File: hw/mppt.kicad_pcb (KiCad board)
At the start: 4 copper layers, 100.1 x 48.6 mm, 79 parts, among them J201 1935776, J301 1935776, J302 1935776, Q301 SW_L, Q302 SW_H, SW201 SW_Push, U201 MCU_Nucleo_L432KC, U401 INA210, U402 INA210, U403 OPA990, U404 OPA990, U501 LMG1210RVRT

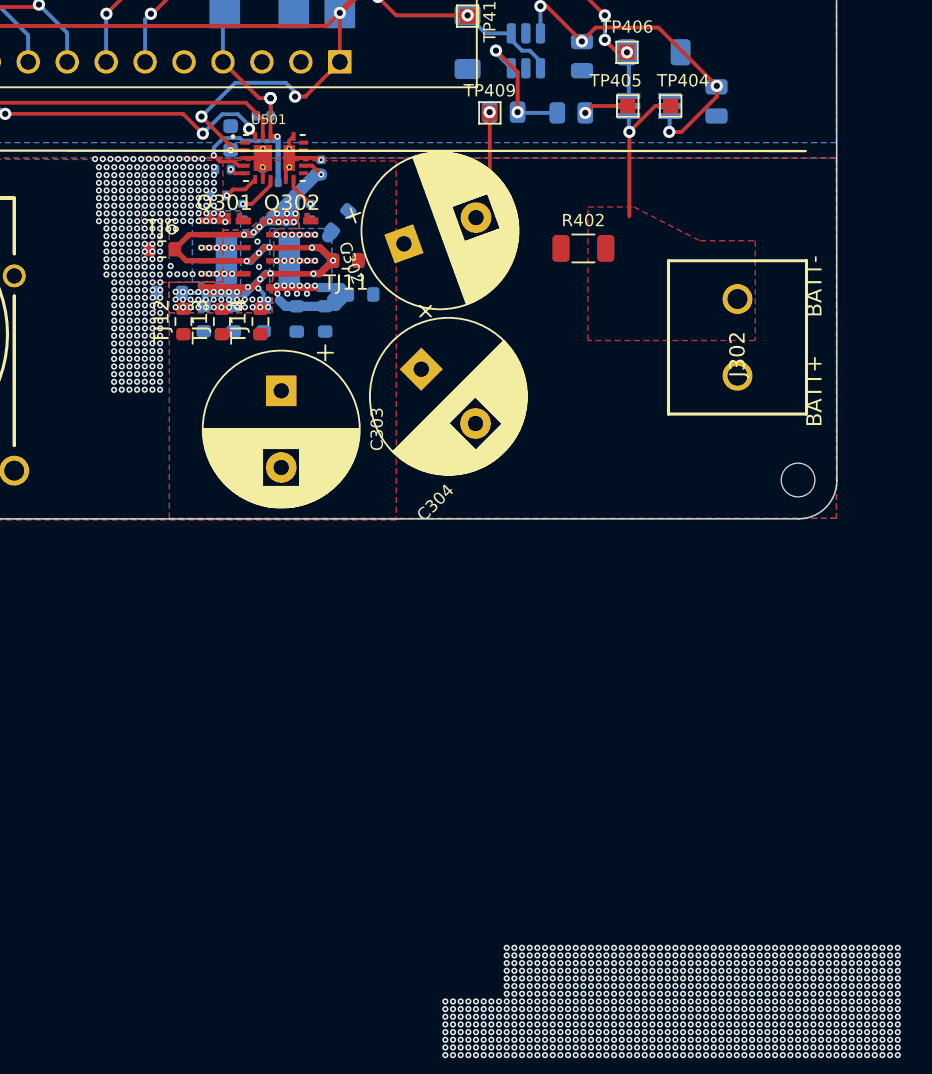
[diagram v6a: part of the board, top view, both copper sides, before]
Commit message: even better thermal design, kept pours out of MOSFET pins and sswitched to 0805 thermal jumpers
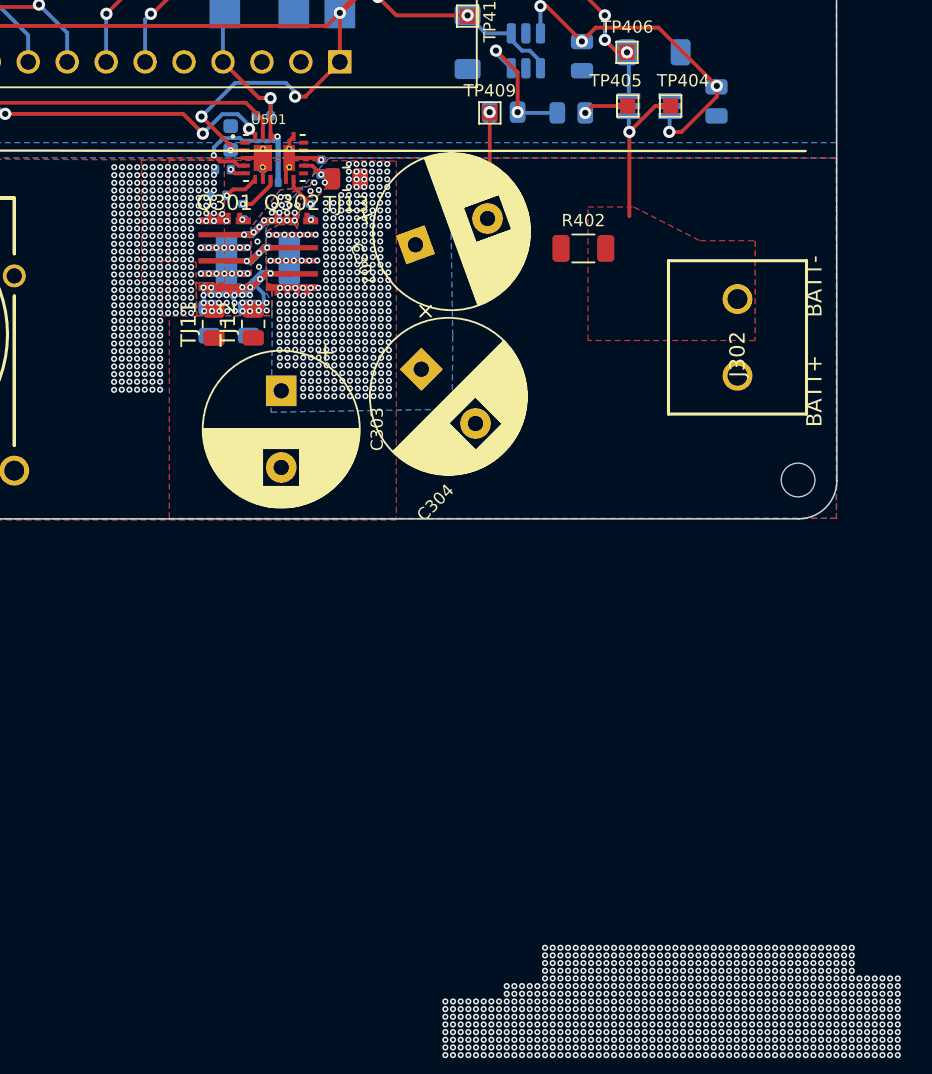
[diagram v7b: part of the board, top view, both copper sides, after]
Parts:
- removed TJ10, TJ14, TJ3, TJ4, TJ5, TJ6, TJ7, TJ8, TJ9: Thermal Jumper, Resistor_SMD:R_0603_1608Metric
- TJ1, TJ11, TJ12, TJ13, TJ2: footprint Resistor_SMD:R_0603_1608Metric -> Resistor_SMD:R_0805_2012Metric
- moved TJ13 12.3 mm to (158.0, 92.9), turned to 180 degrees
- moved TJ11 9.54 mm to (149.4, 102.3), turned to 90 degrees
- moved TJ12 4.55 mm to (152.0, 102.3)
- moved TJ2 0.99 mm to (151.7, 102.2)
- moved C302 0.75 mm to (162.6, 97.2)
- moved TJ1 0.40 mm to (149.1, 102.2)
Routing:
- net /converter/V_SW: track 110.4 -> 69.2 mm, vias 58 -> 59
- net GND: track 31.8 -> 39.0 mm, vias 330 -> 337
- net /converter/V_BATT+: track 12.6 -> 9.94 mm, vias 23 -> 354
- net /converter/SW2: vias 0 -> 1
- net /converter/SW1: vias 0 -> 1
- net +5V: vias 4 -> 3
- net (no net): vias 844 -> 795

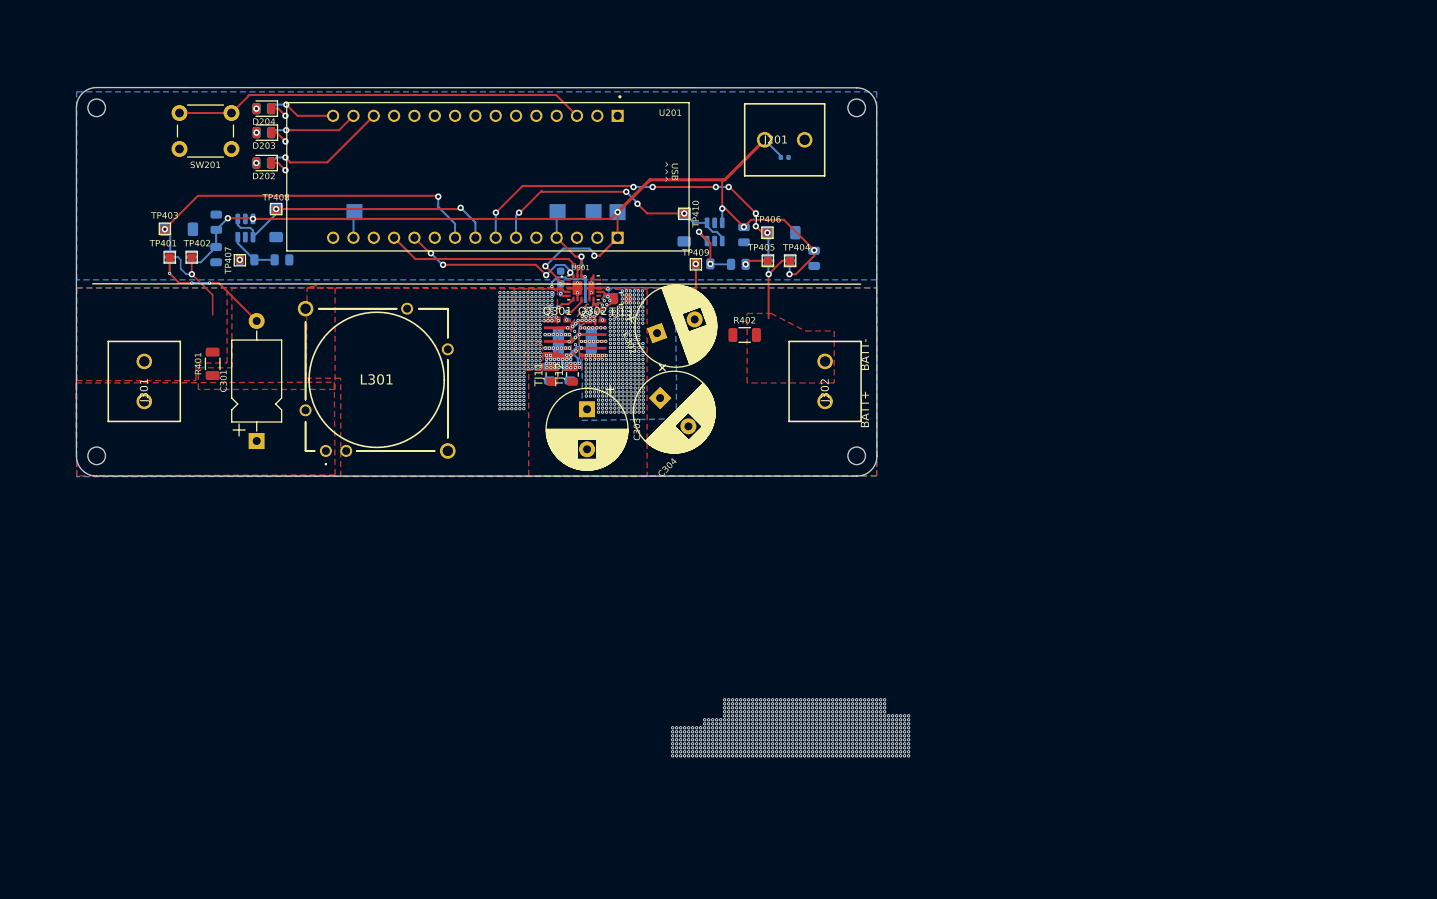
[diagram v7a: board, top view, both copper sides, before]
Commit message: revision of PCB layout
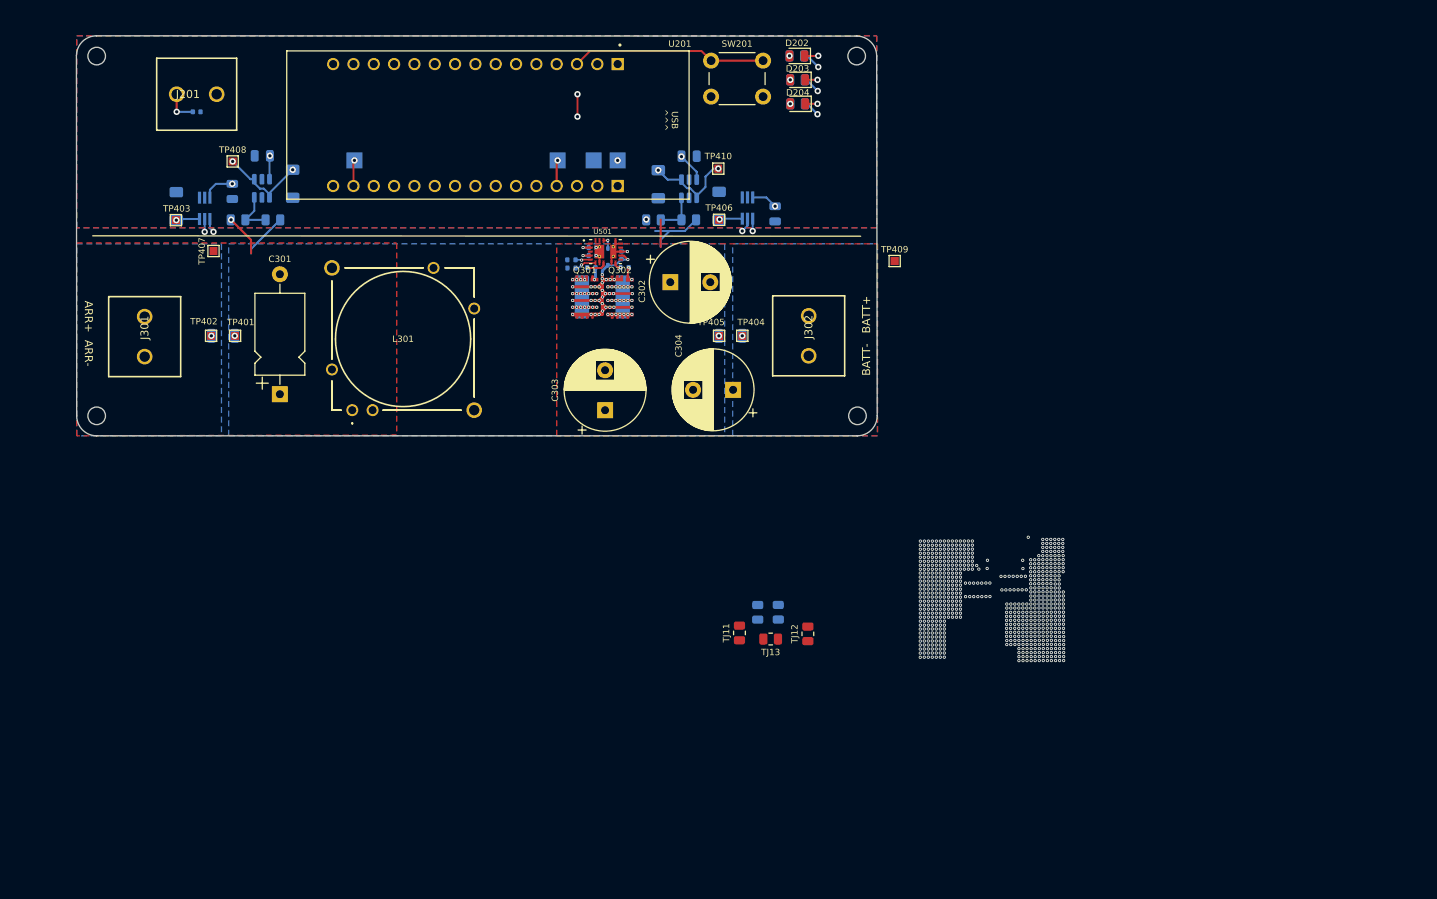
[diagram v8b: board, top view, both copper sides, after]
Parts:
- C1: footprint Capacitor_SMD:C_1812_4532Metric -> Capacitor_SMD:C_2220_5650Metric
- C502: footprint Capacitor_SMD:C_0603_1608Metric -> Capacitor_SMD:C_0402_1005Metric
- R401, R402: moved to B.Cu
- moved C201 73.7 mm to (105.0, 69.5)
- moved J201 73.7 mm to (102.5, 67.3)
- moved D202 68.0 mm to (180.0, 62.5)
- moved R203 68.0 mm to (180.0, 62.5)
- moved D203 67.0 mm to (180.1, 65.5)
- moved R202 67.0 mm to (180.1, 65.5)
- moved SW201 66.8 mm to (175.8, 67.6)
- moved R201 66.7 mm to (180.1, 68.5)
- moved D204 66.7 mm to (180.1, 68.5)
- moved TJ13 46.5 mm to (176.8, 135.4)
- moved TJ12 43.8 mm to (181.4, 134.8)
- moved TJ11 39.9 mm to (172.8, 134.6)
- moved TJ1 39.6 mm to (175.1, 132.1)
- moved TJ2 39.6 mm to (177.7, 132.1)
- moved TP409 24.9 mm to (192.2, 88.2)
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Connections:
- U201 pad 1: unconnected-(U201-D1-Pad1) -> /controller/Heartbeat
- U201 pad 13: /controller/Heartbeat -> unconnected-(U201-D10-Pad13)
- U201 pad 14: /controller/Tracking -> unconnected-(U201-D11-Pad14)
- U201 pad 15: /controller/Error -> unconnected-(U201-D12-Pad15)
- U201 pad 2: unconnected-(U201-D0-Pad2) -> /controller/Tracking
- U201 pad 22: /controller/ARR_CURRENT -> /controller/ARR_VOLTAGE
- U201 pad 23: /controller/ARR_VOLTAGE -> /controller/ARR_CURRENT
- U201 pad 5: unconnected-(U201-D2-Pad5) -> /controller/Error
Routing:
- net +12V: track 126.6 -> 19.9 mm, vias 10 -> 7
- net /converter/V_SW: track 69.2 -> 18.4 mm, vias 59 -> 32
- net /controller/Error: track 8.55 -> 39.8 mm
- net /controller/PWM_EN: track 25.6 -> 0.00 mm
- net /controller/PWM: track 23.2 -> 0.00 mm, vias 4 -> 0
- net /controller/Tracking: track 11.3 -> 31.1 mm
- net /converter/V_ARR+: track 23.6 -> 5.28 mm
- net +5V: track 21.7 -> 6.57 mm
- net GND: track 39.0 -> 52.1 mm, vias 337 -> 357
- net /controller/Heartbeat: track 15.8 -> 28.5 mm
- net /controller/Reset: track 51.8 -> 39.7 mm, vias 0 -> 2
- net /controller/BATT_CURRENT: track 44.7 -> 32.8 mm, vias 8 -> 1
- net /converter/V_BATT+: track 9.94 -> 3.51 mm, vias 354 -> 375
- net /converter/V_BATT-: track 9.94 -> 15.3 mm, vias 1 -> 2
- net /controller/ARR_CURRENT: track 45.1 -> 49.3 mm, vias 2 -> 1
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- added copper zone on F.Cu, net +12V
- added copper zone on B.Cu, net /converter/V_ARR-
- added copper zone on B.Cu, net /converter/V_BATT-
- removed copper zone on F.Cu, net /converter/V_ARR-
- removed copper zone on In1.Cu, net /converter/V_ARR-
- removed copper zone on B.Cu, net /converter/V_BATT+
- removed copper zone on In1.Cu, net /converter/V_BATT+
- removed copper zone on In2.Cu, net /converter/V_BATT+
- removed copper zone on F.Cu, net /converter/V_BATT-
- removed copper zone on In1.Cu, net /converter/V_BATT-
- removed copper zone on B.Cu, net /converter/V_SW
- removed copper zone on F.Cu, net /converter/V_SW
- removed copper zone on In1.Cu, net /converter/V_SW
- removed copper zone on In2.Cu, net /converter/V_SW
- removed copper zone on F.Cu, net GND
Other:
- board size 100.1 x 48.6 mm -> 100.1 x 50 mm
- board text added: "ARR+"
- board text added: "ARR-"
- board text removed: "Gate Driver"
- board text removed: "INCOMPLETE"
- board text removed: "LAYOUT WILL BE REVISED SIGNIFICANTLY"
- board text removed: "PENDING"
